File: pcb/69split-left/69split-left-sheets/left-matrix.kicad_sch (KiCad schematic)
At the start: 60 parts, among them SW10 SW_Push, SW11 SW_Push, SW12 SW_Push, SW13 SW_Push, SW14 SW_Push, SW15 SW_Push, SW16 SW_Push, SW17 SW_Push, SW18 SW_Push, SW19 SW_Push, SW2 SW_Push, SW20 SW_Push, SW21 SW_Push, SW22 SW_Push, SW23 SW_Push, SW24 SW_Push, SW25 SW_Push, SW26 SW_Push, SW27 SW_Push, SW28 SW_Push, SW29 SW_Push, SW3 SW_Push, SW30 SW_Push, SW31 SW_Push, SW4 SW_Push, SW5 SW_Push, SW6 SW_Push, SW7 SW_Push, SW8 SW_Push, SW9 SW_Push

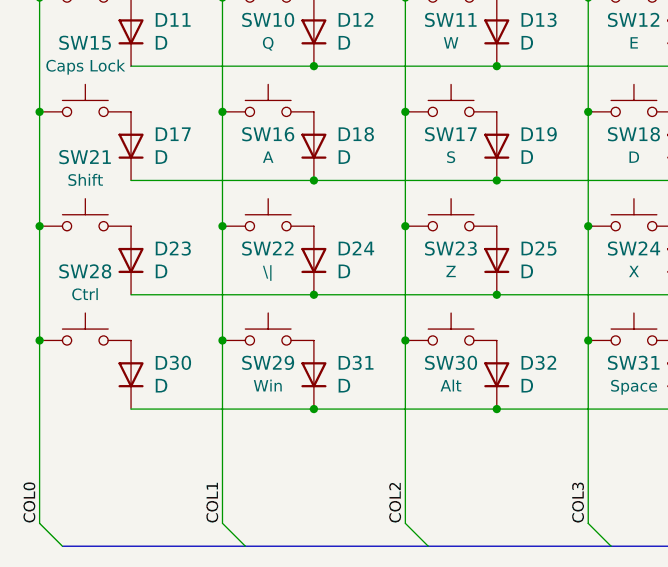
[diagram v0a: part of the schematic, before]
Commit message: Update key names
Change Win to GUI and specify L/R Alt, L/R Shift, and L/R Ctrl
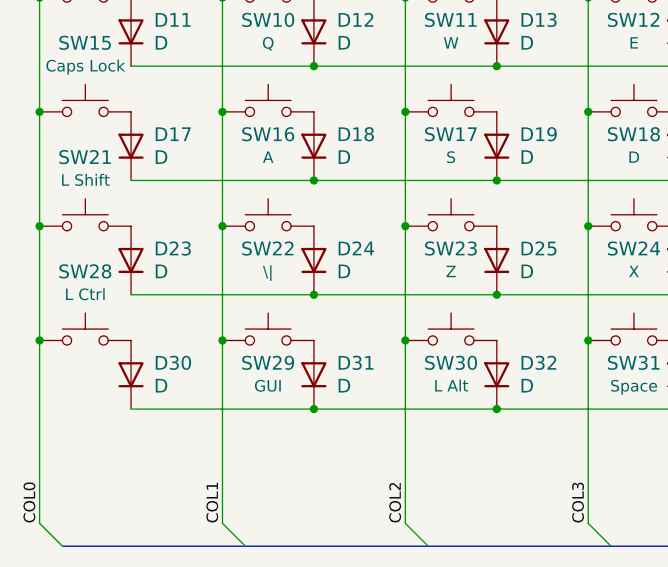
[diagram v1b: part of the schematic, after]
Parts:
- SW21: Key Shift -> L Shift
- SW28: Key Ctrl -> L Ctrl
- SW29: Key Win -> GUI
- SW30: Key Alt -> L Alt
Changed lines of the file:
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@@
 			)
 		)
-		(property "Key" "Win"
+		(property "Key" "GUI"
 			(at 86.36 125.73 0)
 			(effects
@@
 			)
 		)
-		(property "Key" "Shift"
+		(property "Key" "L Shift"
 			(at 66.04 102.87 0)
 			(effects
@@
 			)
 		)
-		(property "Key" "Alt"
+		(property "Key" "L Alt"
 			(at 106.68 125.73 0)
 			(effects
@@
 			)
 		)
-		(property "Key" "Ctrl"
+		(property "Key" "L Ctrl"
 			(at 66.04 115.57 0)
 			(effects
